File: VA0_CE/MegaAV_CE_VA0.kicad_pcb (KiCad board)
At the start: 4 copper layers, 50 x 50 mm, 155 parts, among them CN1 MD-90SM_MD2, IC1 CXA1645/CXA2075/BH7236AF, P1 SMD_Conn_01x01, U2 NCV8114ASN250T1G, U3 TS924, U6 TS922, U7 TS924

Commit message: MegaAV VA0 CE PCBA updates
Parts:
- added G***: LOGO, MyLibrary:RIP-Felix Logo(Small), B.Cu at (194.4, 140.9)
- U3, U7: footprint Package_SO:TSSOP-14_4.4x5mm_P0.65mm -> Package_SO:SO-14_3.9x8.65mm_P1.27mm
- U6: footprint Package_SO:TSSOP-8_4.4x3mm_P0.65mm -> Package_SO:SO-8_3.9x4.9mm_P1.27mm
- moved C9 11.9 mm to (187.3, 116.4), turned to 0 degrees
- moved R48 7.83 mm to (200.9, 113.2)
- moved R53 7.44 mm to (200.4, 114.5)
- moved C14 7.19 mm to (190.5, 118.8)
- moved C42 6.01 mm to (193.5, 110.6), turned to 180 degrees
- moved C12 5.97 mm to (190.6, 121.5), turned to 180 degrees
- moved R47 4.58 mm to (200.6, 115.5)
- moved R4 4.54 mm to (190.6, 122.6), turned to 180 degrees
- moved C15 4.51 mm to (201.9, 125.6)
- moved U3 4.01 mm to (195.4, 125.9)
- moved C35 3.45 mm to (200.6, 116.5)
- moved C11 3.22 mm to (191.3, 126.7), turned to 90 degrees
- moved U7 3.07 mm to (195.6, 116.7)
- moved R7 2.93 mm to (191.3, 124.1)
- moved C13 1.89 mm to (194.6, 131.6)
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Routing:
- net +5V: track 183.0 -> 168.8 mm, vias 12 -> 10
- net Net-(C42-Pad1): track 3.52 -> 13.2 mm, vias 0 -> 2
- net Net-(U3A-+): track 3.92 -> 13.5 mm, vias 0 -> 2
- net Net-(FMR_2-C): track 13.0 -> 20.9 mm
- net /V_REF: track 72.5 -> 65.6 mm
- net Net-(U3B--): track 8.54 -> 15.4 mm, vias 0 -> 2
- net Net-(FMR_1-C): track 21.9 -> 28.2 mm, vias 0 -> 5
- net Net-(SR3-Pin_1): track 30.4 -> 35.7 mm
- net Net-(SL3-Pin_1): track 33.4 -> 38.1 mm
- net Net-(C3-Pad2): track 11.7 -> 16.2 mm
- net /SR: track 37.4 -> 33.8 mm
- net Net-(U3A--): track 3.91 -> 7.44 mm
- net Net-(U3B-+): track 3.87 -> 7.38 mm
- net Net-(C46-Pad1): track 13.5 -> 10.5 mm
- net Net-(C43-Pad1): track 2.33 -> 5.31 mm
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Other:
- board text added: "TS922"

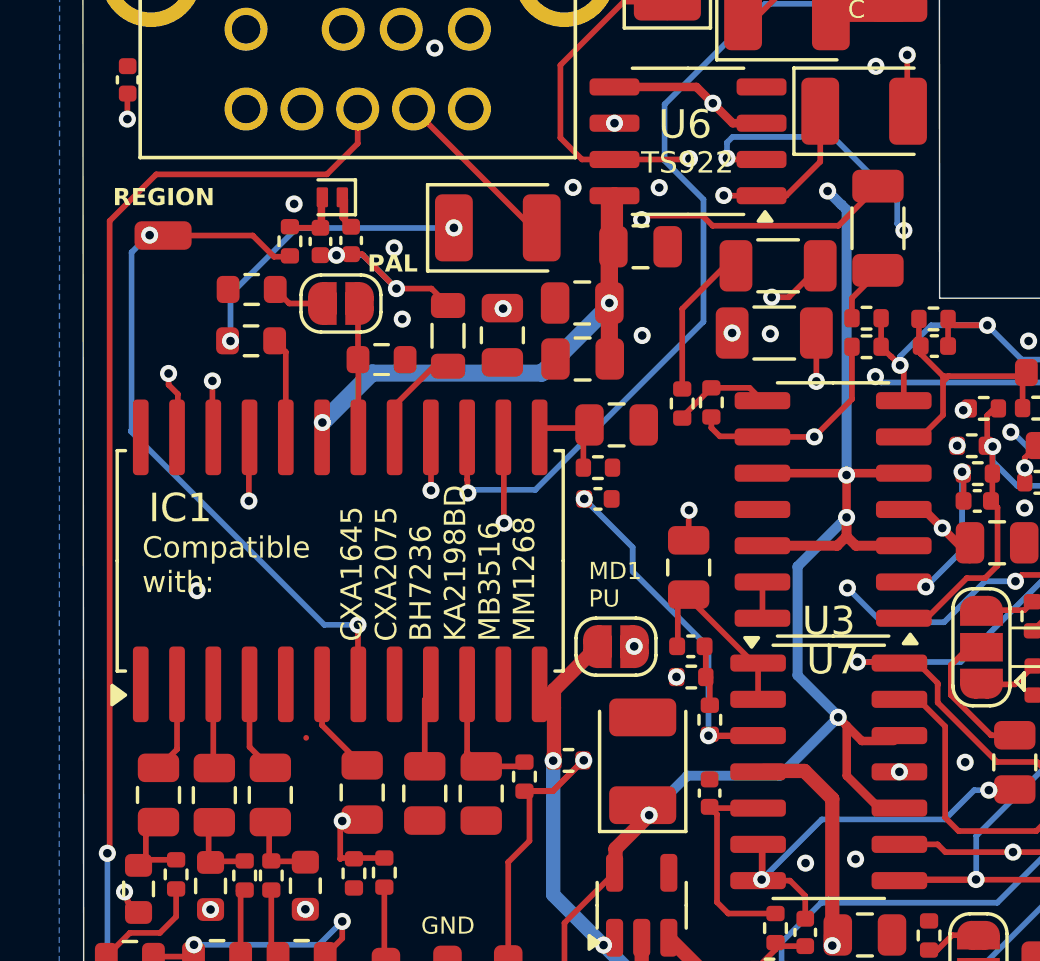
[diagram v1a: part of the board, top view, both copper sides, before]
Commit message: Fixed VA0 errors
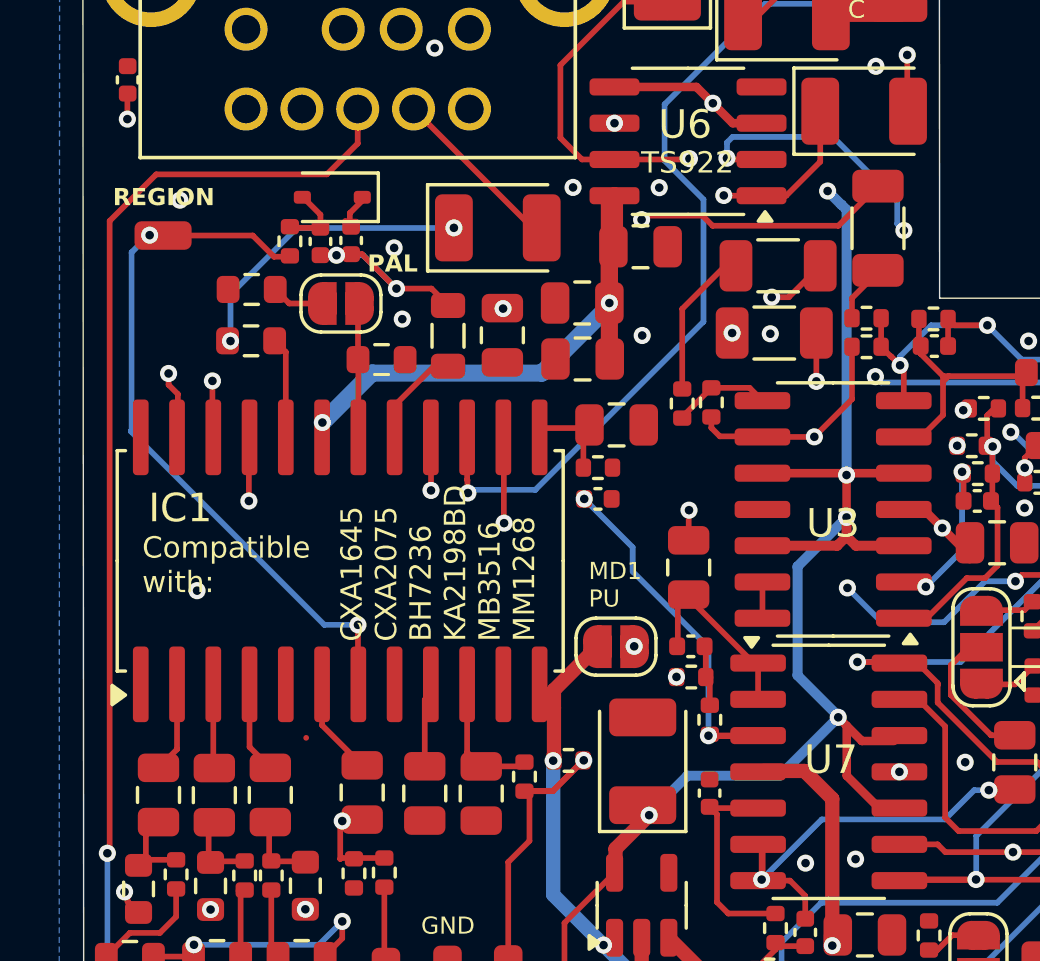
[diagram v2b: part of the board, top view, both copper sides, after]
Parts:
- D2: footprint Diode_SMD:D_SOD-882 -> Diode_SMD:D_SOD-323
- moved G*** 0.16 mm to (194.5, 140.8)
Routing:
- net GND: track 40.7 -> 40.0 mm
- net Net-(D2-A): track 3.16 -> 2.50 mm
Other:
- board text added: "rev.VA0"
- board text removed: "rev.VA2"
